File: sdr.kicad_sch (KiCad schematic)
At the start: 9 parts, among them U1 IS42S86400F-7TL

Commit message: [#100650] Add rev number
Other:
- moved on the sheet: C1, C2, C3, C4, C5, C6, C7, C8, U1

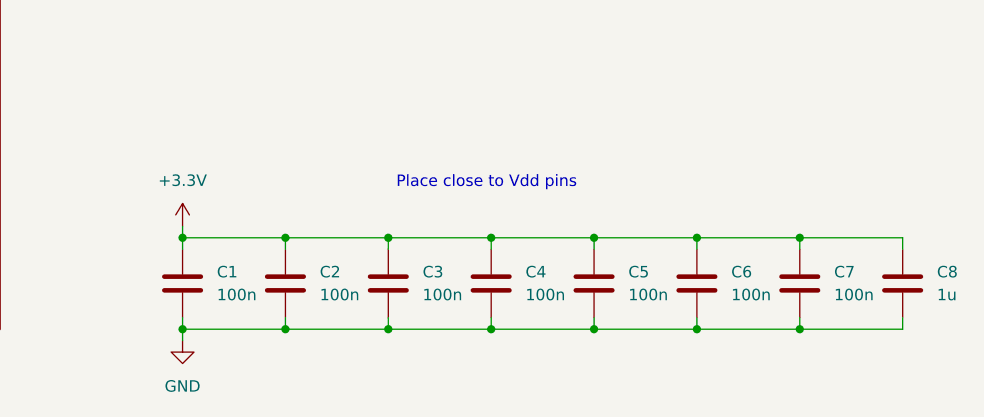
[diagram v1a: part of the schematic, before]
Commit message: [#100650] Add EEPROM memory IC for Serial Presence Detection
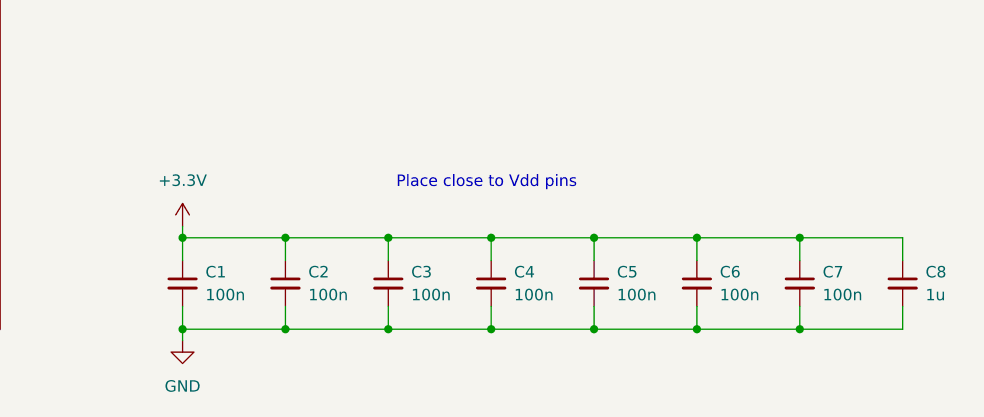
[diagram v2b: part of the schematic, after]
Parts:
- removed C1, C2, C3, C4, C5, C6, C7: 100n, antmicro-footprints:C_0402_1005Metric, symbol Device:C
- removed C8: 1u, antmicro-footprints:C_0402_1005Metric, symbol Device:C
- added C1, C2, C3, C4, C5, C6, C7: C_100n_0402, antmicro-footprints:C_0402_1005Metric, symbol antmicroCapacitors0402:C_100n_0402
- added C8: C_1u_0402, antmicro-footprints:C_0402_1005Metric, symbol antmicroCapacitors0402:C_1u_0402
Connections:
- net +3.3V: now also C1.1, C2.1, C3.1, C4.1, C5.1, C6.1, C7.1, C8.1
- net GND: now also C1.2, C2.2, C3.2, C4.2, C5.2, C6.2, C7.2, C8.2

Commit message: [#100650] Update schematic labels, add bulk cap
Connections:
- net NCAS renamed ~{CAS}
- net NCS renamed ~{CS}
- net NRAS renamed ~{RAS}
- net NWE renamed ~{WE}

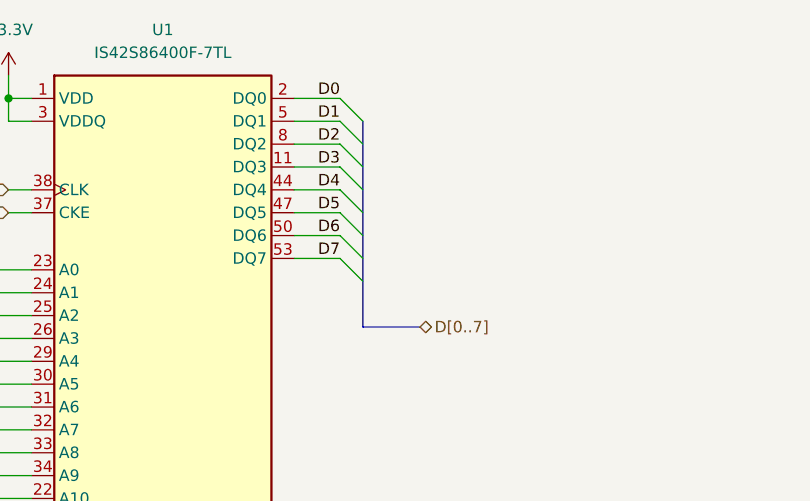
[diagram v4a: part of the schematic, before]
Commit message: [#100919] Route data bus
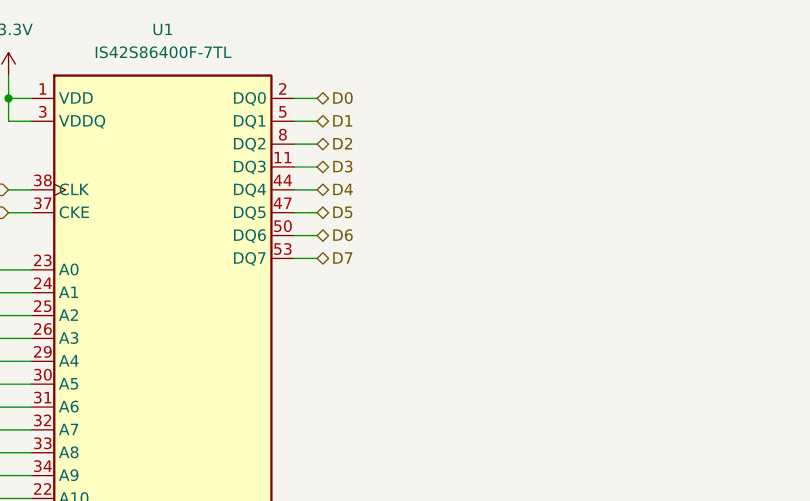
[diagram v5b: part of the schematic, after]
